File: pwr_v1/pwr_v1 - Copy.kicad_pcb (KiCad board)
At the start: 4 copper layers, 166 x 166 mm, 196 parts, among them CN11 Conn_02x36_Odd_Even, CN12 Conn_02x36_Odd_Even, J1 Conn_01x12_Pin, M1 Conn_01x08_Socket, M2 Conn_01x08_Socket, M3 Conn_01x08_Socket, M4 Conn_01x08_Socket, M5 Conn_01x08_Socket, Q1 BSS84, U1 LM2576S-5, U2 LM2576S-12, U3 LM2576S-3.3, U4 LSM6DSLTR

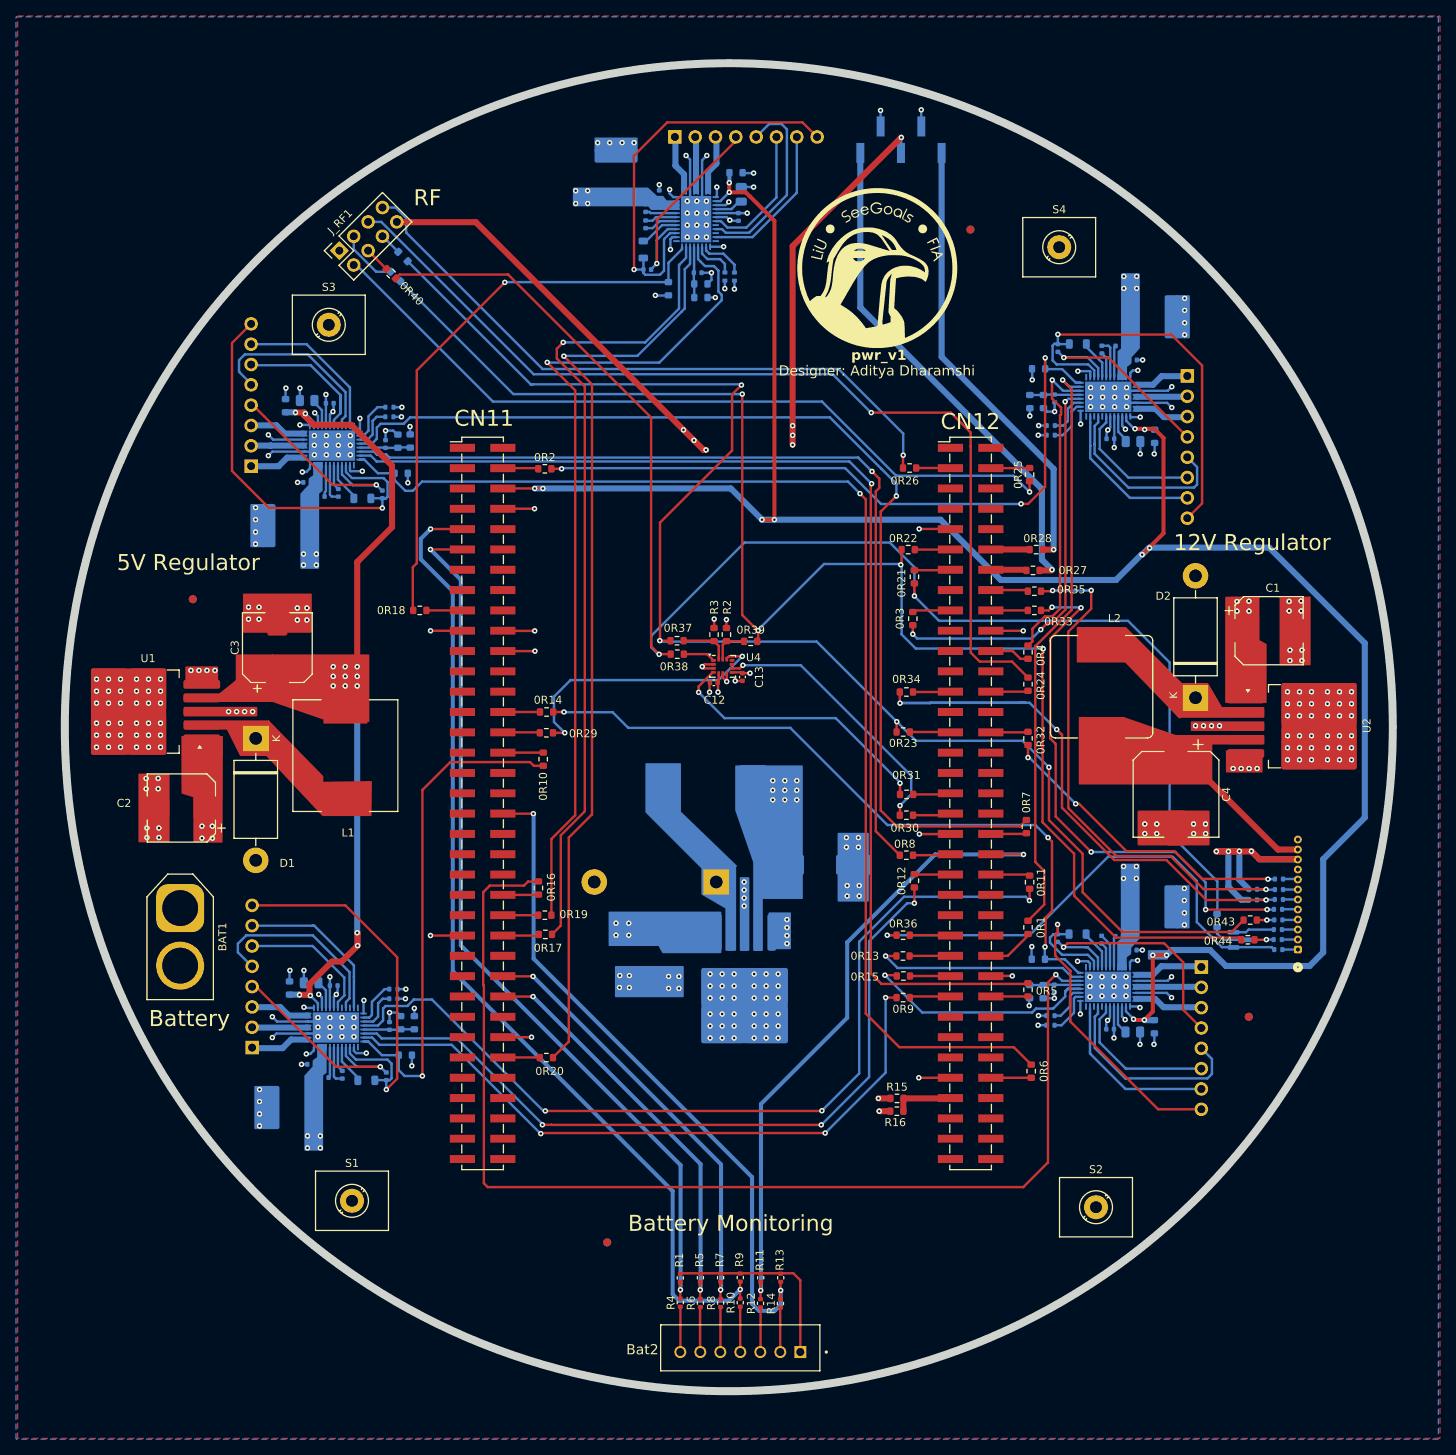
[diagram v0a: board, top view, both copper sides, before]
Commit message: Sch: DNP updated, JLC part numbers updated for all components; Lay: Fiducial placement, routing aligned.
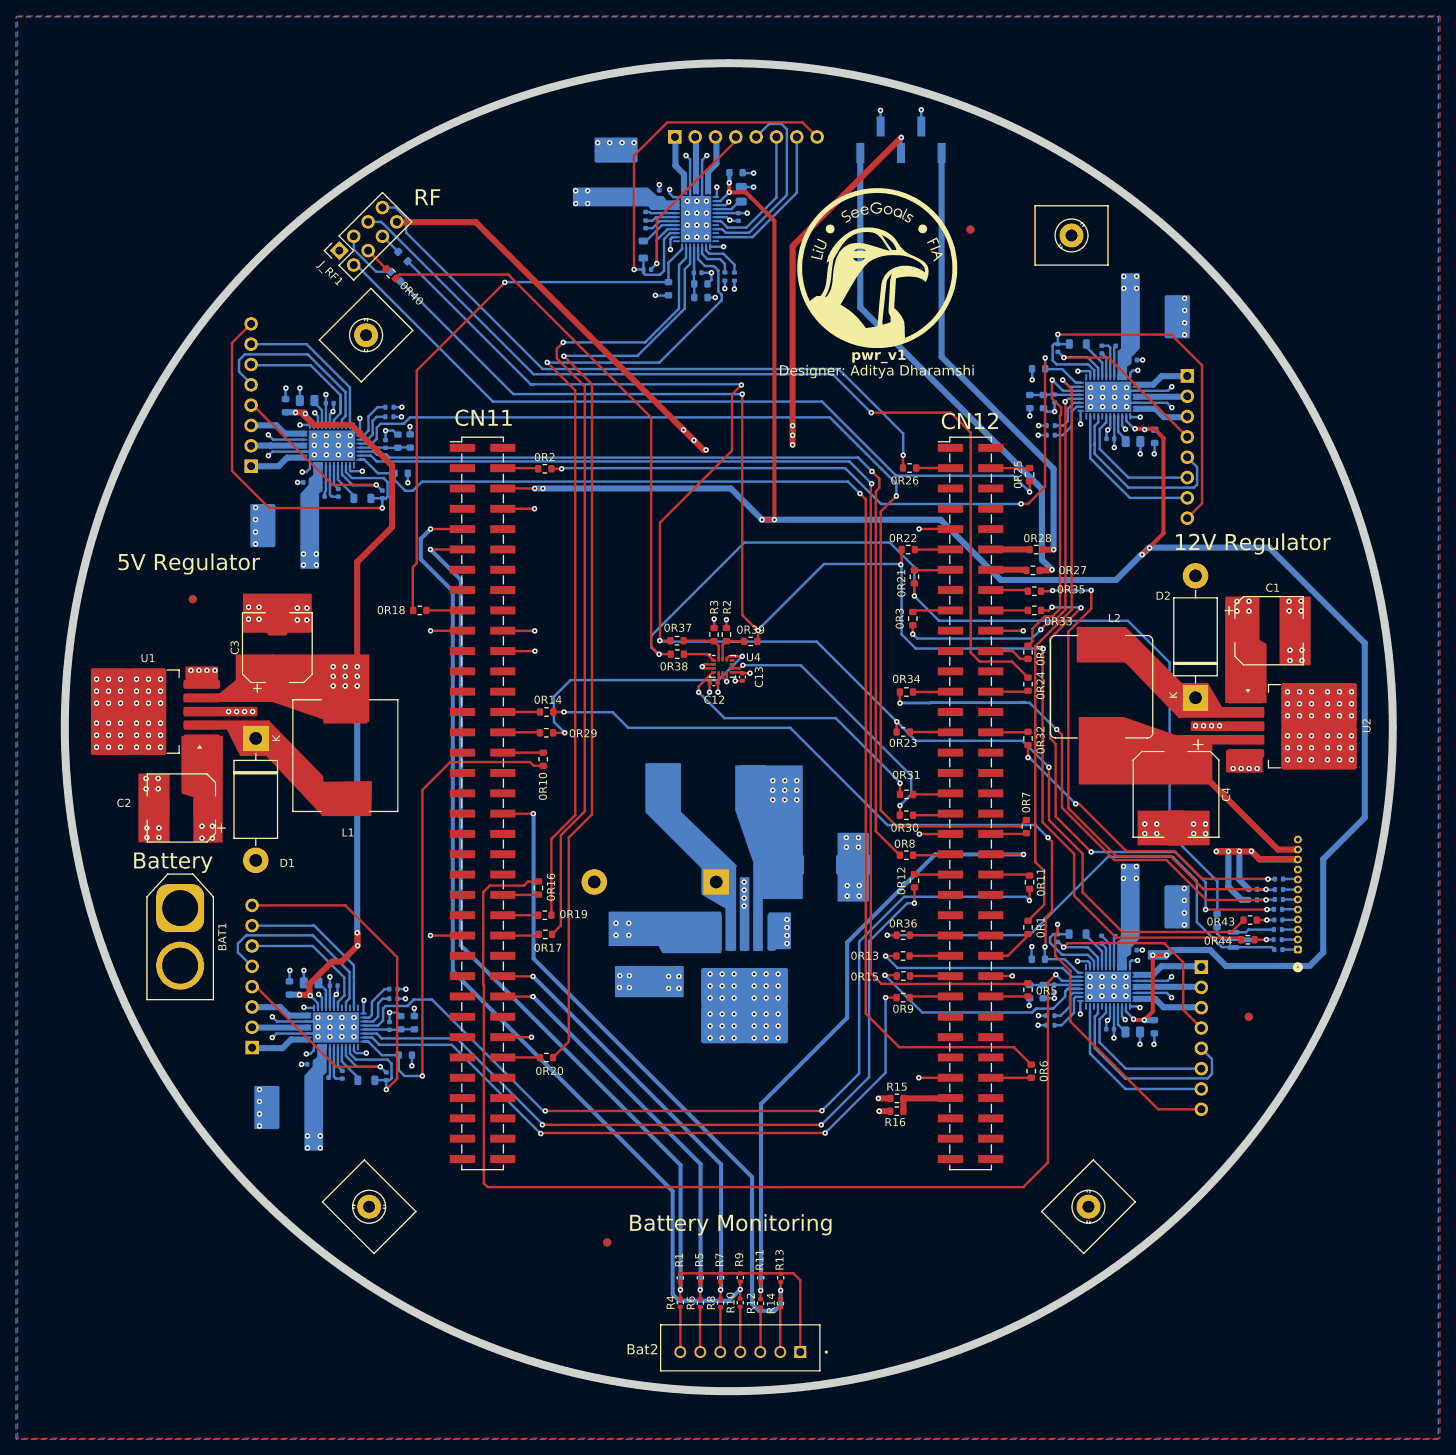
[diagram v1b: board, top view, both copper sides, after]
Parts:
- removed the FID1 at (83.0, 84.0)
- removed FID4, FID5, FID6, FID7, FID8: Fiducial, Fiducial:Fiducial_1mm_Mask3mm
- added ?: , , B.Cu at (215.0, 136.2)
- added ?: , , B.Cu at (180.2, 37.8)
- added ?: , , B.Cu at (134.8, 164.4)
- added ?: , , B.Cu at (83.0, 84.0)
- added FID1: Fiducial, Fiducial:Fiducial_1mm_Mask2mm, F.Cu at (180.2, 37.8)
- added FID1: Fiducial, Fiducial:Fiducial_1mm_Mask2mm, F.Cu at (83.0, 84.0)
- 1U1, 2U1, 3U1, 4U1, 5U1: value MCT8316Z0TRGFR -> MCT8316Z0TQRGFRQ1
- FID2: footprint Fiducial:Fiducial_1mm_Mask3mm -> Fiducial:Fiducial_1mm_Mask2mm; moved to F.Cu
- FID3: footprint Fiducial:Fiducial_1mm_Mask3mm -> Fiducial:Fiducial_1mm_Mask2mm
- moved FID2 141.9 mm to (215.0, 136.2), turned to 0 degrees
- moved S2 121.5 mm to (192.8, 38.5)
- moved S4 120.0 mm to (195.0, 159.9), turned to -135 degrees
- moved S3 110.4 mm to (105.0, 159.9), turned to 135 degrees
- moved S1 108.2 mm to (104.7, 51.0), turned to 45 degrees
